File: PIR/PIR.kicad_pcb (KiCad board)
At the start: 2 copper layers, 50 x 80 mm, 31 parts, among them J2 PIR, J3 BUS, Q1 BC846, Q2 BC846, Q3 BC857, SW1 tamper switch, U1 AP63203WU, U2 WT8266-S1

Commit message: upgrades people, upgrades!
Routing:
- net +12V: track 171.6 -> 172.5 mm
- net "reset": track 84.1 -> 84.7 mm
- net +3.3V: track 214.2 -> 214.8 mm
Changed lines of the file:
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@@
     (pts (xy 100 130) (xy 150 130))
     (height 17.32)
-    (gr_text "50,0000 mm" (at 125 145.52) (layer "F.Cu")
+    (gr_text "50.0000 mm" (at 125 145.52) (layer "F.Cu")
       (effects (font (size 1.5 1.5) (thickness 0.3)))
     )
@@
     (pts (xy 150 130) (xy 150 50))
     (height 27.8)
-    (gr_text "80,0000 mm" (at 176 90 90) (layer "F.Cu")
+    (gr_text "80.0000 mm" (at 176 90 90) (layer "F.Cu")
       (effects (font (size 1.5 1.5) (thickness 0.3)))
     )
@@
   (segment (start 110 79.755) (end 111.825 81.58) (width 0.25) (layer "B.Cu") (net 2))
   (segment (start 133.74 126.74) (end 134.5 127.5) (width 0.25) (layer "F.Cu") (net 3))
-  (segment (start 111 56.5) (end 116.680698 56.5) (width 0.25) (layer "F.Cu") (net 3))
-  (segment (start 111.825 79.04) (end 108.285 75.5) (width 0.25) (layer "F.Cu") (net 3))
+  (segment (start 116.680698 56.5) (end 118.180698 58) (width 0.25) (layer "F.Cu") (net 3))
   (segment (start 133.74 124) (end 133.74 126.74) (width 0.25) (layer "F.Cu") (net 3))
+  (segment (start 105.25 75.5) (end 102 72.25) (width 0.25) (layer "F.Cu") (net 3))
   (segment (start 143 125.138) (end 143 125.1375) (width 0.25) (layer "F.Cu") (net 3))
   (segment (start 143.5 127.5) (end 144 127) (width 0.25) (layer "F.Cu") (net 3))
-  (segment (start 129.425 58) (end 131.825 60.4) (width 0.25) (layer "F.Cu") (net 3))
-  (segment (start 108.285 75.5) (end 105.25 75.5) (width 0.25) (layer "F.Cu") (net 3))
+  (segment (start 118.180698 58) (end 129.425 58) (width 0.25) (layer "F.Cu") (net 3))
+  (segment (start 102 72.25) (end 102 64) (width 0.25) (layer "F.Cu") (net 3))
   (segment (start 145.675 126) (end 145.5 125.825) (width 0.25) (layer "F.Cu") (net 3))
-  (segment (start 102 65.5) (end 111 56.5) (width 0.25) (layer "F.Cu") (net 3))
-  (segment (start 102 72.25) (end 102 65.5) (width 0.25) (layer "F.Cu") (net 3))
+  (segment (start 111.825 79.04) (end 108.285 75.5) (width 0.25) (layer "F.Cu") (net 3))
   (segment (start 144 127) (end 144 125.188) (width 0.25) (layer "F.Cu") (net 3))
   (segment (start 143 127.5) (end 143.5 127.5) (width 0.25) (layer "F.Cu") (net 3))
@@
   (segment (start 145.5 125.825) (end 144.6375 125.825) (width 0.25) (layer "F.Cu") (net 3))
   (segment (start 144 125.1875) (end 144 125.188) (width 0.25) (layer "F.Cu") (net 3))
+  (segment (start 108.285 75.5) (end 105.25 75.5) (width 0.25) (layer "F.Cu") (net 3))
+  (segment (start 129.425 58) (end 131.825 60.4) (width 0.25) (layer "F.Cu") (net 3))
   (segment (start 143.95 125.1375) (end 144 125.1875) (width 0.25) (layer "F.Cu") (net 3))
   (segment (start 135 105.5) (end 139.8 105.5) (width 0.25) (layer "F.Cu") (net 3))
   (segment (start 148 126) (end 145.675 126) (width 0.25) (layer "F.Cu") (net 3))
   (segment (start 138.5 93) (end 136.1175 93) (width 0.25) (layer "F.Cu") (net 3))
-  (segment (start 116.680698 56.5) (end 118.180698 58) (width 0.25) (layer "F.Cu") (net 3))
+  (segment (start 102 64) (end 109.5 56.5) (width 0.25) (layer "F.Cu") (net 3))
+  (segment (start 109.5 56.5) (end 116.680698 56.5) (width 0.25) (layer "F.Cu") (net 3))
   (segment (start 133.74 106.76) (end 135 105.5) (width 0.25) (layer "F.Cu") (net 3))
   (segment (start 134.5 127.5) (end 143 127.5) (width 0.25) (layer "F.Cu") (net 3))
   (segment (start 144 125.188) (end 144.132 125.32) (width 0.25) (layer "F.Cu") (net 3))
   (segment (start 144.6375 125.825) (end 143.95 125.1375) (width 0.25) (layer "F.Cu") (net 3))
-  (segment (start 105.25 75.5) (end 102 72.25) (width 0.25) (layer "F.Cu") (net 3))
-  (segment (start 118.180698 58) (end 129.425 58) (width 0.25) (layer "F.Cu") (net 3))
   (segment (start 133.74 124) (end 133.74 106.76) (width 0.25) (layer "F.Cu") (net 3))
   (via (at 138.5 93) (size 0.8) (drill 0.4) (layers "F.Cu" "B.Cu") (net 3))
@@
   (segment (start 141.5 116.5) (end 141.5 115.425) (width 1) (layer "F.Cu") (net 6))
   (segment (start 131.5 126.5) (end 131.5 98.666726) (width 1) (layer "F.Cu") (net 6))
+  (segment (start 110.675 60.325) (end 106.5 64.5) (width 1) (layer "F.Cu") (net 6))
   (segment (start 142 125.1375) (end 140.1375 125.1375) (width 1) (layer "F.Cu") (net 6))
   (segment (start 107.26 128) (end 130 128) (width 1) (layer "F.Cu") (net 6))
@@
   (segment (start 139.925 115.425) (end 141.5 115.425) (width 1) (layer "F.Cu") (net 6))
   (segment (start 131.5 98.666726) (end 126.413274 93.58) (width 1) (layer "F.Cu") (net 6))
-  (segment (start 107.4875 63.4875) (end 107.5125 63.4875) (width 1) (layer "F.Cu") (net 6))
   (segment (start 114 74) (end 114 73) (width 1) (layer "F.Cu") (net 6))
   (segment (start 119.38 89.38) (end 119.38 85.1) (width 1) (layer "F.Cu") (net 6))
   (segment (start 114 73) (end 114 72) (width 1) (layer "F.Cu") (net 6))
   (segment (start 114 74.237792) (end 114 74) (width 1) (layer "F.Cu") (net 6))
+  (segment (start 105.5 64.5) (end 104.225 65.775) (width 1) (layer "F.Cu") (net 6))
+  (segment (start 115.5 60.325) (end 110.675 60.325) (width 1) (layer "F.Cu") (net 6))
   (segment (start 115 75.237792) (end 114 74.237792) (width 1) (layer "F.Cu") (net 6))
   (segment (start 130 128) (end 131.5 126.5) (width 1) (layer "F.Cu") (net 6))
   (segment (start 140 123.5) (end 140 122) (width 1) (layer "F.Cu") (net 6))
   (segment (start 116 83.5) (end 114 83.5) (width 1) (layer "F.Cu") (net 6))
-  (segment (start 107.5125 63.4875) (end 110.675 60.325) (width 1) (layer "F.Cu") (net 6))
   (segment (start 141.5 62) (end 141.5 67.5) (width 1) (layer "F.Cu") (net 6))
-  (segment (start 107.4875 63.4875) (end 104.225 66.75) (width 1) (layer "F.Cu") (net 6))
   (segment (start 104.43 125.17) (end 107.26 128) (width 1) (layer "F.Cu") (net 6))
+  (segment (start 104.225 65.775) (end 104.225 66.75) (width 1) (layer "F.Cu") (net 6))
   (segment (start 116 83.5) (end 115 83.5) (width 1) (layer "F.Cu") (net 6))
   (segment (start 125 93.58) (end 123.58 93.58) (width 1) (layer "F.Cu") (net 6))
@@
   (segment (start 115 83.5) (end 115 75.237792) (width 1) (layer "F.Cu") (net 6))
   (segment (start 104.43 125.17) (end 104.43 118.67) (width 1) (layer "F.Cu") (net 6))
+  (segment (start 106.5 64.5) (end 105.5 64.5) (width 1) (layer "F.Cu") (net 6))
   (segment (start 140 122) (end 140 118) (width 1) (layer "F.Cu") (net 6))
   (segment (start 123.58 93.58) (end 119.38 89.38) (width 1) (layer "F.Cu") (net 6))
@@
   (segment (start 140.1375 125.1375) (end 140 125) (width 1) (layer "F.Cu") (net 6))
   (segment (start 104.225 66.75) (end 104.225 68.5) (width 1) (layer "F.Cu") (net 6))
-  (segment (start 110.675 60.325) (end 115.5 60.325) (width 1) (layer "F.Cu") (net 6))
   (via (at 114 74) (size 0.8) (drill 0.4) (layers "F.Cu" "B.Cu") (net 6))
   (via (at 140 122) (size 0.8) (drill 0.4) (layers "F.Cu" "B.Cu") (net 6))
@@
   (segment (start 114 67) (end 109.5 62.5) (width 1) (layer "B.Cu") (net 6))
   (segment (start 140 122) (end 140 125) (width 1) (layer "B.Cu") (net 6))
-  (segment (start 103 69.025) (end 103 66) (width 0.25) (layer "F.Cu") (net 7))
   (segment (start 104.225 70.25) (end 103 69.025) (width 0.25) (layer "F.Cu") (net 7))
   (segment (start 135.5 78.2368) (end 135.5 82.5) (width 0.25) (layer "F.Cu") (net 7))
   (segment (start 116.32 57.595) (end 115.5 57.595) (width 0.25) (layer "F.Cu") (net 7))
   (segment (start 137.2368 76.5) (end 135.5 78.2368) (width 0.25) (layer "F.Cu") (net 7))
-  (segment (start 111.405 57.595) (end 115.5 57.595) (width 0.25) (layer "F.Cu") (net 7))
+  (segment (start 103 69.025) (end 103 65) (width 0.25) (layer "F.Cu") (net 7))
+  (segment (start 103 65) (end 110.405 57.595) (width 0.25) (layer "F.Cu") (net 7))
   (segment (start 119.125 60.4) (end 116.32 57.595) (width 0.25) (layer "F.Cu") (net 7))
   (segment (start 143 91.5) (end 143.5 91) (width 0.25) (layer "F.Cu") (net 7))
   (segment (start 115.5 58.675) (end 115.5 58) (width 0.25) (layer "F.Cu") (net 7))
   (segment (start 137.2368 76.5) (end 139.5 76.5) (width 0.25) (layer "F.Cu") (net 7))
-  (segment (start 103 66) (end 111.405 57.595) (width 0.25) (layer "F.Cu") (net 7))
+  (segment (start 110.405 57.595) (end 115.5 57.595) (width 0.25) (layer "F.Cu") (net 7))
   (segment (start 143.5 91) (end 143.5 84.5) (width 0.25) (layer "F.Cu") (net 7))
   (segment (start 115.5 58) (end 115.5 57.595) (width 0.25) (layer "F.Cu") (net 7))

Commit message: upgrades people, upgrades!
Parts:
- moved R1 0.32 mm to (137.7, 86.0)
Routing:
- net +12V: track 172.5 -> 173.7 mm
- net Net-(BZ1--): track 3.97 -> 4.93 mm

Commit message: upgrades people, upgrades!
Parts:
- added 3.3V: TestPoint, TestPoint:TestPoint_Pad_1.5x1.5mm, F.Cu at (119.0, 80.5)
- renumbered FLASH to J1, BATTERY to J4
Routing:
- net +3.3V: track 214.8 -> 218.3 mm

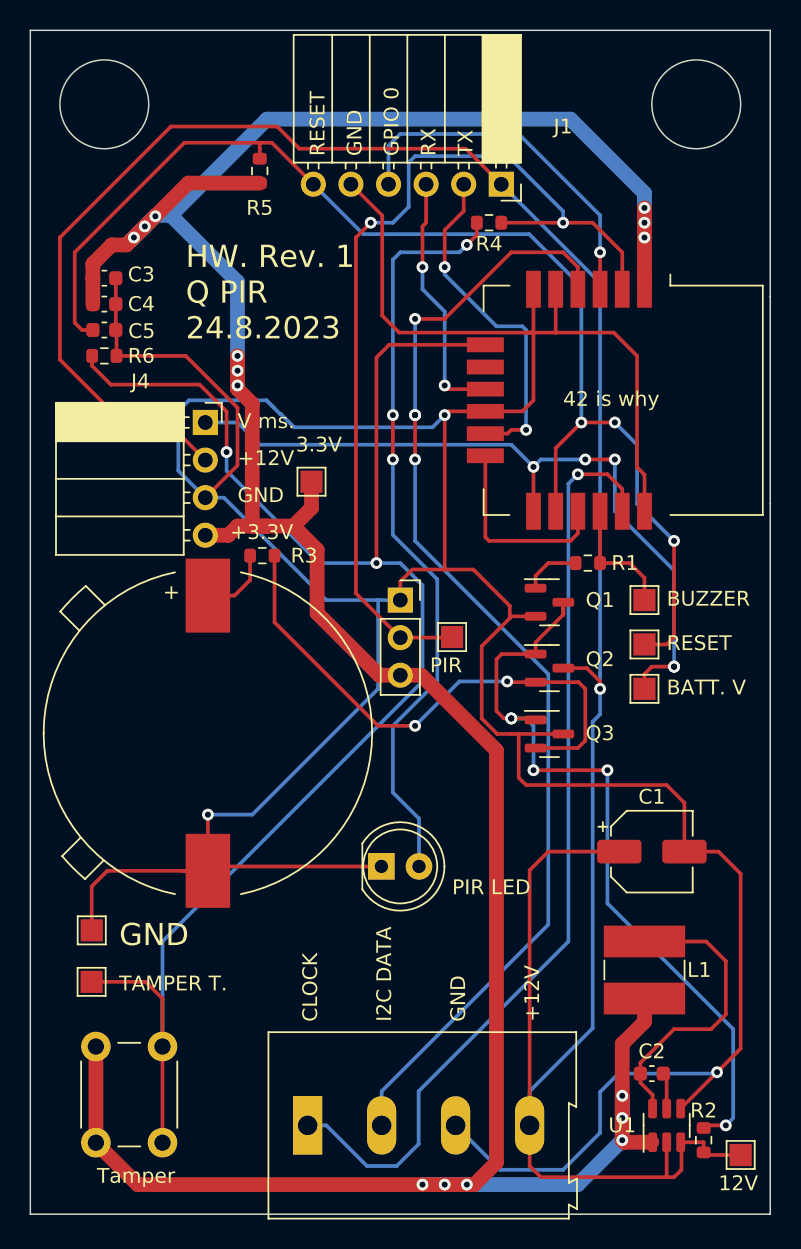
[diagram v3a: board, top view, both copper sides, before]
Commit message: Update symbol and footprint of WT8266
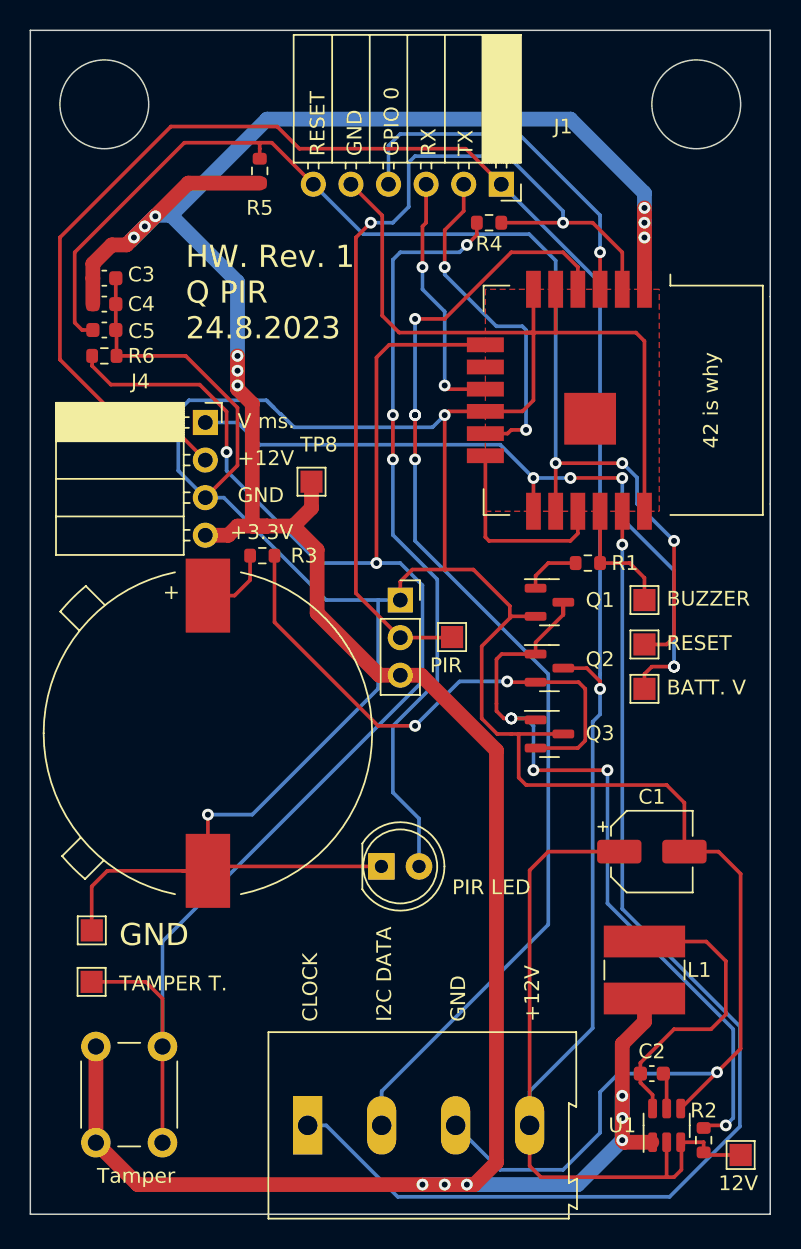
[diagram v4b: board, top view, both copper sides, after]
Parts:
- renumbered 3.3V to TP8
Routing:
- net clock: track 63.9 -> 78.0 mm
- net "reset": track 85.1 -> 83.0 mm
- net battery voltage: track 51.5 -> 49.4 mm
- net GND: track 272.4 -> 273.2 mm
- added copper zone on F.Cu, net GND

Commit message: Fix incident
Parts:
- moved L1 0.50 mm to (142.0, 113.5), turned to 180 degrees
- moved C2 0.22 mm to (142.2, 120.5), turned to 0 degrees
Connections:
- C2 pad 1: Net-(U1-SW) -> Net-(U1-BST)
- C2 pad 2: Net-(U1-BST) -> Net-(U1-SW)
- L1 pad 1: Net-(U1-BST) -> Net-(U1-SW)
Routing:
- net Net-(U1-BST): track 20.2 -> 2.61 mm
- net Net-(U1-SW): track 2.46 -> 9.97 mm
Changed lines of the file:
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@@
   )
   (footprint "Capacitor_SMD:C_0603_1608Metric" (layer "F.Cu")
-    (at 142 120.5 180)
+    (at 142.225 120.5)
     (descr "Capacitor SMD 0603 (1608 Metric), square (rectangular) end terminal, IPC_7351 nominal, (Body size source: IPC-SM-782 page 76, https://www.pcb-3d.com/wordpress/wp-content/uploads/ipc-sm-782a_amendment_1_and_2.pdf), generated with kicad-footprint-generator")
     (tags "capacitor")
@@
     (property "ki_keywords" "cap capacitor")
     (attr smd)
-    (fp_text reference "C2" (at 0 1.5 180) (layer "F.SilkS")
+    (fp_text reference "C2" (at 0 -1.5) (layer "F.SilkS")
         (effects (font (size 1 1) (thickness 0.15)))
     )
-    (fp_text value "100n" (at 0 1.43 180) (layer "F.Fab")
+    (fp_text value "100n" (at 0 1.43) (layer "F.Fab")
         (effects (font (size 1 1) (thickness 0.15)))
     )
-    (fp_text user "${REFERENCE}" (at 0 0 180) (layer "F.Fab")
+    (fp_text user "${REFERENCE}" (at 0 0) (layer "F.Fab")
         (effects (font (size 0.4 0.4) (thickness 0.06)))
     )
@@
     (fp_line (start 0.8 0.4) (end -0.8 0.4)
       (stroke (width 0.1) (type solid)) (layer "F.Fab"))
-    (pad "1" smd roundrect (at -0.775 0 180) (size 0.9 0.95) (layers "F.Cu" "F.Paste" "F.Mask") (roundrect_rratio 0.25)
-      (net 4 "Net-(U1-SW)") (pintype "passive"))
-    (pad "2" smd roundrect (at 0.775 0 180) (size 0.9 0.95) (layers "F.Cu" "F.Paste" "F.Mask") (roundrect_rratio 0.25)
+    (pad "1" smd roundrect (at -0.775 0) (size 0.9 0.95) (layers "F.Cu" "F.Paste" "F.Mask") (roundrect_rratio 0.25)
       (net 5 "Net-(U1-BST)") (pintype "passive"))
+    (pad "2" smd roundrect (at 0.775 0) (size 0.9 0.95) (layers "F.Cu" "F.Paste" "F.Mask") (roundrect_rratio 0.25)
+      (net 4 "Net-(U1-SW)") (pintype "passive"))
     (model "${KICAD6_3DMODEL_DIR}/Capacitor_SMD.3dshapes/C_0603_1608Metric.wrl"
       (offset (xyz 0 0 0))
@@
   )
   (footprint "Inductor_SMD:L_Ferrocore_DLG-0504" (layer "F.Cu")
-    (at 141.5 113.5 -90)
+    (at 142 113.5 180)
     (descr "Ferrocore DLG-0504 unshielded SMD power inductor, 5.8x5.2x4.5mm, https://www.tme.eu/Document/bda580f72a60a2225c2f6576c2740ae1/dlg-0504.pdf")
     (tags "smd inductor dlg-0504")
@@
     (property "ki_keywords" "inductor choke coil reactor magnetic")
     (attr smd)
-    (fp_text reference "L1" (at 0 -3.7 -180) (layer "F.SilkS")
+    (fp_text reference "L1" (at -2 -4 90) (layer "F.SilkS")
         (effects (font (size 1 1) (thickness 0.15)))
     )
-    (fp_text value "4u7" (at 0 3.7 90) (layer "F.Fab")
+    (fp_text value "4u7" (at 0 3.7) (layer "F.Fab")
         (effects (font (size 1 1) (thickness 0.15)))
     )
-    (fp_text user "${REFERENCE}" (at 0 0 90) (layer "F.Fab")
+    (fp_text user "${REFERENCE}" (at 0 0) (layer "F.Fab")
         (effects (font (size 1 1) (thickness 0.15)))
     )
@@
     (fp_arc (start 0.85 -2.6) (mid 2.9 0) (end 0.85 2.6)
       (stroke (width 0.1) (type solid)) (layer "F.Fab"))
-    (pad "1" smd rect (at -1.925 0 270) (size 2.15 5.5) (layers "F.Cu" "F.Paste" "F.Mask")
-      (net 5 "Net-(U1-BST)") (pinfunction "1") (pintype "passive"))
-    (pad "2" smd rect (at 1.925 0 270) (size 2.15 5.5) (layers "F.Cu" "F.Paste" "F.Mask")
+    (pad "1" smd rect (at -1.925 0 180) (size 2.15 5.5) (layers "F.Cu" "F.Paste" "F.Mask")
+      (net 4 "Net-(U1-SW)") (pinfunction "1") (pintype "passive"))
+    (pad "2" smd rect (at 1.925 0 180) (size 2.15 5.5) (layers "F.Cu" "F.Paste" "F.Mask")
       (net 6 "+3.3V") (pinfunction "2") (pintype "passive"))
     (model "${KICAD6_3DMODEL_DIR}/Inductor_SMD.3dshapes/L_Ferrocore_DLG-0504.wrl"
@@
     )
   )
-  (dimension (type aligned) (layer "F.Cu")
-    (pts (xy 100 130) (xy 150 130))
-    (height 17.32)
-    (gr_text "50,0000 mm" (at 125 145.52) (layer "F.Cu")
-      (effects (font (size 1.5 1.5) (thickness 0.3)))
-    )
-    (format (prefix "") (suffix "") (units 3) (units_format 1) (precision 4))
-    (style (thickness 0.2) (arrow_length 1.27) (text_position_mode 0) (extension_height 0.58642) (extension_offset 0.5) keep_text_aligned)
-  )
-  (dimension (type aligned) (layer "F.Cu")
-    (pts (xy 150 130) (xy 150 50))
-    (height 27.8)
-    (gr_text "80,0000 mm" (at 176 90 90) (layer "F.Cu")
-      (effects (font (size 1.5 1.5) (thickness 0.3)))
-    )
-    (format (prefix "") (suffix "") (units 3) (units_format 1) (precision 4))
-    (style (thickness 0.2) (arrow_length 1.27) (text_position_mode 0) (extension_height 0.58642) (extension_offset 0.5) keep_text_aligned)
-  )
   (segment (start 114.85 87.15) (end 114.85 85.5) (width 0.25) (layer "F.Cu") (net 1))
   (segment (start 112 88.2) (end 113.8 88.2) (width 0.25) (layer "F.Cu") (net 1))
@@
   (segment (start 138 96.7223) (end 138.5 96.2223) (width 0.25) (layer "B.Cu") (net 3))
   (segment (start 138.5 93.5) (end 138.5 67.075) (width 0.25) (layer "B.Cu") (net 3))
-  (segment (start 143 120.725) (end 142.775 120.5) (width 0.25) (layer "F.Cu") (net 4))
-  (segment (start 143 122.8625) (end 143 120.725) (width 0.25) (layer "F.Cu") (net 4))
-  (segment (start 147 112.9) (end 145.675 111.575) (width 0.25) (layer "F.Cu") (net 5))
-  (segment (start 142.05 121.9375) (end 141.225 121.1125) (width 0.25) (layer "F.Cu") (net 5))
-  (segment (start 142.05 122.8625) (end 142.05 121.9375) (width 0.25) (layer "F.Cu") (net 5))
-  (segment (start 147 116.5) (end 147 112.9) (width 0.25) (layer "F.Cu") (net 5))
-  (segment (start 141.225 121.1125) (end 141.225 120.5) (width 0.25) (layer "F.Cu") (net 5))
-  (segment (start 141.225 119.775) (end 141.225 120.5) (width 0.25) (layer "F.Cu") (net 5))
-  (segment (start 145.675 111.575) (end 141.5 111.575) (width 0.25) (layer "F.Cu") (net 5))
-  (segment (start 143.5 117.5) (end 146 117.5) (width 0.25) (layer "F.Cu") (net 5))
-  (segment (start 143.5 117.5) (end 141.225 119.775) (width 0.25) (layer "F.Cu") (net 5))
-  (segment (start 146 117.5) (end 147 116.5) (width 0.25) (layer "F.Cu") (net 5))
+  (segment (start 143.925 113.5) (end 143.925 119.575) (width 1) (layer "F.Cu") (net 4))
+  (segment (start 143.925 119.575) (end 143 120.5) (width 1) (layer "F.Cu") (net 4))
+  (segment (start 143 120.275) (end 143 122.8625) (width 0.5) (layer "F.Cu") (net 4))
+  (segment (start 142.05 122.8625) (end 142.05 121.1) (width 0.25) (layer "F.Cu") (net 5))
+  (segment (start 142.05 121.1) (end 141.45 120.5) (width 0.25) (layer "F.Cu") (net 5))
   (segment (start 113.38 84.12) (end 111.825 84.12) (width 1) (layer "F.Cu") (net 6))
   (segment (start 126.413274 93.58) (end 125 93.58) (width 1) (layer "F.Cu") (net 6))
-  (segment (start 140 122) (end 140 118.5) (width 1) (layer "F.Cu") (net 6))
   (segment (start 131.5 126.5) (end 131.5 98.666726) (width 1) (layer "F.Cu") (net 6))
   (segment (start 110.675 60.325) (end 106.5 64.5) (width 1) (layer "F.Cu") (net 6))
@@
   (segment (start 107.26 128) (end 130 128) (width 1) (layer "F.Cu") (net 6))
   (segment (start 117.78 83.5) (end 116 83.5) (width 1) (layer "F.Cu") (net 6))
-  (segment (start 139.925 115.425) (end 141.5 115.425) (width 1) (layer "F.Cu") (net 6))
   (segment (start 131.5 98.666726) (end 126.413274 93.58) (width 1) (layer "F.Cu") (net 6))
   (segment (start 114 74) (end 114 73) (width 1) (layer "F.Cu") (net 6))
@@
   (segment (start 114 74.237792) (end 114 74) (width 1) (layer "F.Cu") (net 6))
   (segment (start 105.5 64.5) (end 104.225 65.775) (width 1) (layer "F.Cu") (net 6))
-  (segment (start 140 118.5) (end 141.5 117) (width 1) (layer "F.Cu") (net 6))
   (segment (start 117.78 83.5) (end 119 82.28) (width 1) (layer "F.Cu") (net 6))
   (segment (start 115.5 60.325) (end 110.675 60.325) (width 1) (layer "F.Cu") (net 6))
@@
   (segment (start 116 83.5) (end 114 83.5) (width 1) (layer "F.Cu") (net 6))
   (segment (start 141.5 62) (end 141.5 67.5) (width 1) (layer "F.Cu") (net 6))
-  (segment (start 141.5 117) (end 141.5 115.425) (width 1) (layer "F.Cu") (net 6))
   (segment (start 104.43 125.17) (end 107.26 128) (width 1) (layer "F.Cu") (net 6))
   (segment (start 104.225 65.775) (end 104.225 66.75) (width 1) (layer "F.Cu") (net 6))
@@
   (segment (start 140.1375 125.1375) (end 140 125) (width 1) (layer "F.Cu") (net 6))
   (segment (start 104.225 66.75) (end 104.225 68.5) (width 1) (layer "F.Cu") (net 6))
+  (segment (start 140 122) (end 140 113.575) (width 1) (layer "F.Cu") (net 6))
   (segment (start 119 82.28) (end 119 80.5) (width 1) (layer "F.Cu") (net 6))
+  (segment (start 140 113.575) (end 140.075 113.5) (width 1) (layer "F.Cu") (net 6))
   (via (at 114 74) (size 0.8) (drill 0.4) (layers "F.Cu" "B.Cu") (net 6))
   (via (at 140 122) (size 0.8) (drill 0.4) (layers "F.Cu" "B.Cu") (net 6))
